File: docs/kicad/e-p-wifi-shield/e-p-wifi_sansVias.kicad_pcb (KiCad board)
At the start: 2 copper layers, 76.2 x 86.4 mm, 49 parts, among them J1 Shunt, J2 Vbat1, J3 Masse T1, J4 Température, J5 Vbat2, J6 Conn_02x14_MKR1010, SW1 StSp - Farnell 986-501, SW2 Sleep - Farnell 986-501, SW3 Conrad 711771, SW4 BP APEM - Farnell 108-2512

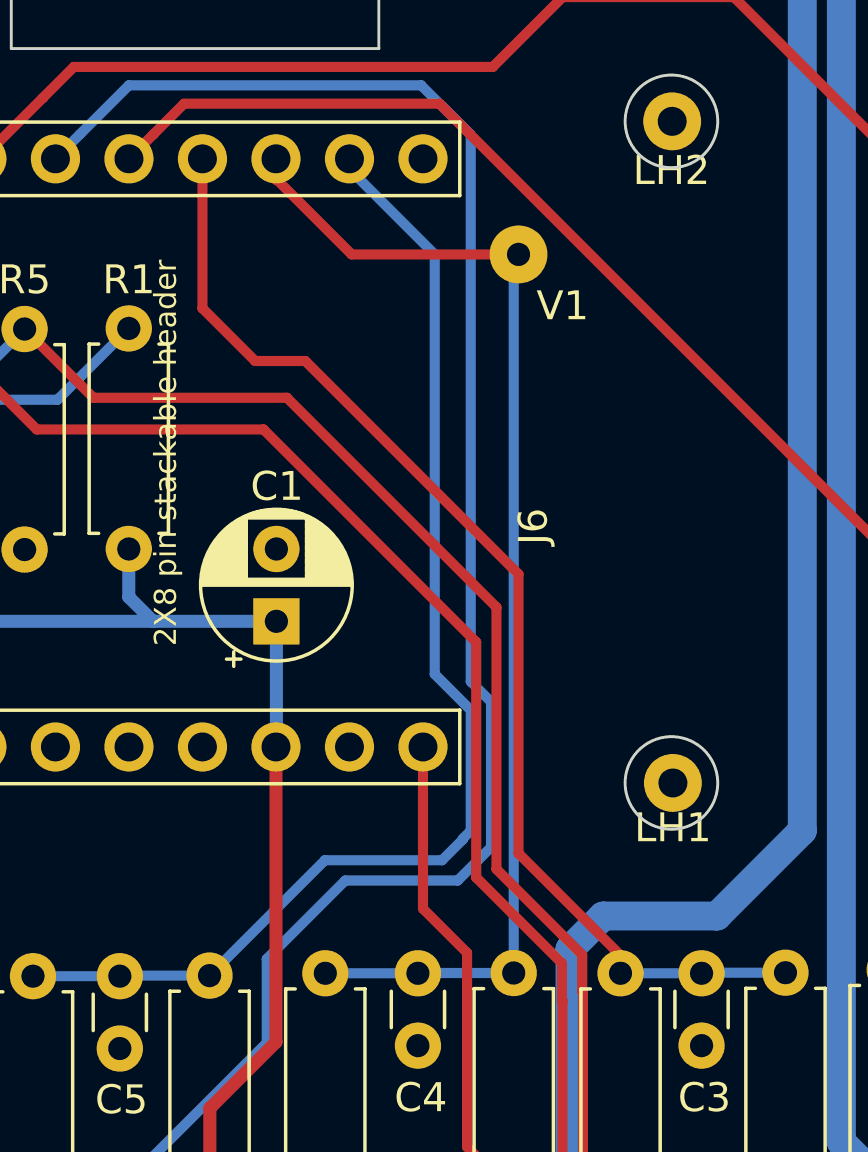
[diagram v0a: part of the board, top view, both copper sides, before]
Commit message: update schema and pcb without via
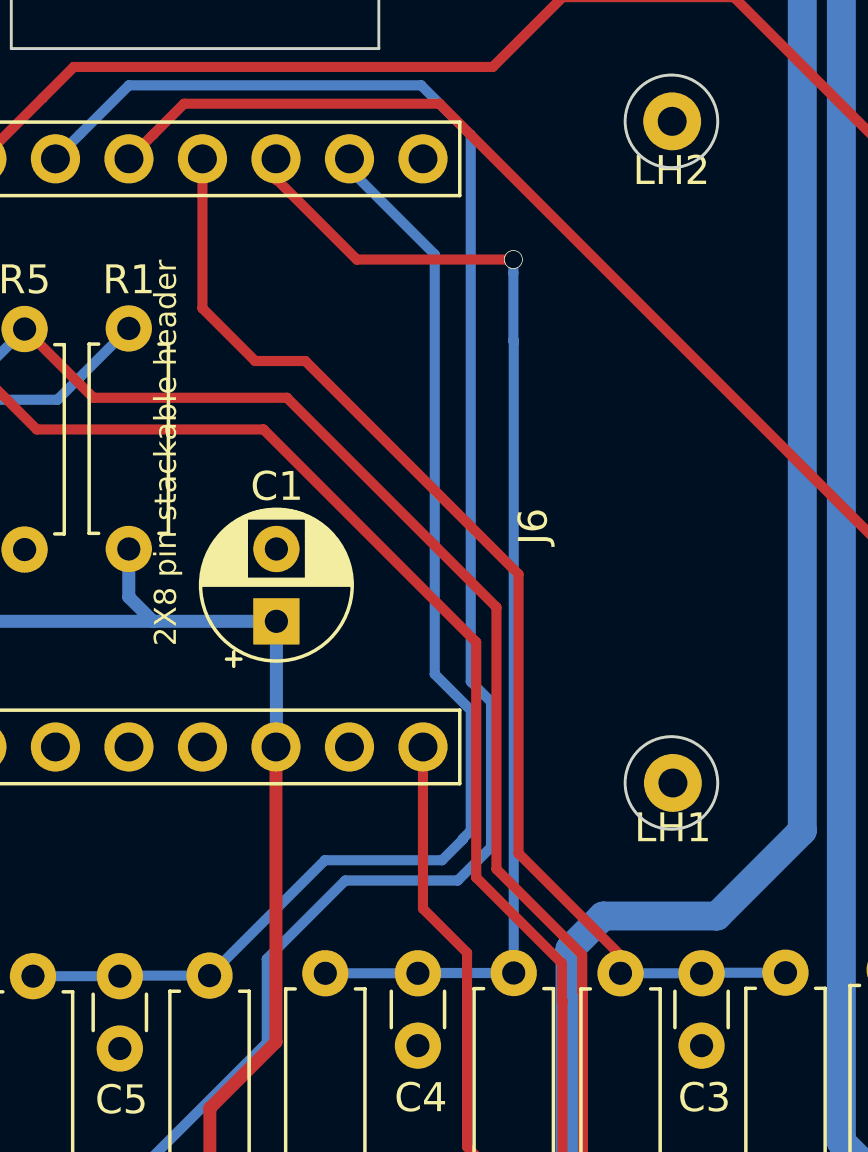
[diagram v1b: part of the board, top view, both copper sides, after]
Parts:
- removed V1: Via, e-p-wifi-v2:Via-DIY
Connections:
- SW4 pad 3: (no net) -> GND
- SW4 pad 4: (no net) -> GND
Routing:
- net Net-(C4-Pad1): track 42.3 -> 42.0 mm, vias 0 -> 1
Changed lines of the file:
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@@
     (thickness 1.6)
     (drawings 43)
-    (tracks 245)
+    (tracks 249)
     (zones 0)
-    (modules 49)
+    (modules 48)
     (nets 38)
   )
@@
     (fp_line (start 3.81 0) (end 3.81 7.62) (layer F.SilkS) (width 0.12))
     (fp_line (start -3.81 0) (end 3.81 0) (layer F.SilkS) (width 0.12))
-    (pad 3 thru_hole circle (at -2.54 5.08) (size 1.524 1.524) (drill 0.8) (layers *.Cu *.Mask))
-    (pad 4 thru_hole circle (at 2.54 5.08) (size 1.524 1.524) (drill 0.8) (layers *.Cu *.Mask))
+    (pad 3 thru_hole circle (at -2.54 5.08) (size 1.524 1.524) (drill 0.8) (layers *.Cu *.Mask)
+      (net 2 GND))
+    (pad 4 thru_hole circle (at 2.54 5.08) (size 1.524 1.524) (drill 0.8) (layers *.Cu *.Mask)
+      (net 2 GND))
     (pad 2 thru_hole circle (at 2.54 0) (size 1.524 1.524) (drill 0.8) (layers *.Cu *.Mask)
       (net 37 "Net-(C6-Pad1)"))
     (pad 1 thru_hole circle (at -2.54 0) (size 1.524 1.524) (drill 0.8) (layers *.Cu *.Mask)
       (net 1 +3V3))
-  )
-  (module e-p-wifi-v2:Via-DIY (layer F.Cu)
-    (at 70.866 61.722)
-    (descr "CP, Axial series, Axial, Horizontal, pin pitch=15mm, , length*diameter=10*4.5mm^2, Electrolytic Capacitor, , http://www.vishay.com/docs/28325/021asm.pdf")
-    (tags "CP Axial series Axial Horizontal pin pitch 15mm  length 10mm diameter 4.5mm Electrolytic Capacitor")
-    (fp_text reference V1 (at 1.524 1.778) (layer F.SilkS)
-      (effects (font (size 1 1) (thickness 0.15)))
-    )
-    (fp_text value Via (at 3.81 1.27) (layer F.Fab)
-      (effects (font (size 1 1) (thickness 0.15)))
-    )
-    (fp_text user %R (at 3.81 0) (layer F.Fab)
-      (effects (font (size 1 1) (thickness 0.15)))
-    )
-    (pad 1 thru_hole oval (at 0 0) (size 2 2) (drill 0.8) (layers *.Cu *.Mask)
-      (net 5 "Net-(C4-Pad1)"))
-    (model ${KISYS3DMOD}/Capacitor_THT.3dshapes/CP_Axial_L10.0mm_D4.5mm_P15.00mm_Horizontal.wrl
-      (at (xyz 0 0 0))
-      (scale (xyz 1 1 1))
-      (rotate (xyz 0 0 0))
-    )
   )
   (module e-p-wifi-v2:Via-DIY (layer F.Cu)
@@
   (segment (start 67.39 86.56) (end 64.19 86.56) (width 0.35) (layer B.Cu) (net 5))
   (segment (start 62.485 59.148541) (end 62.485 58.42) (width 0.35) (layer F.Cu) (net 5))
-  (segment (start 70.7 61.888) (end 70.866 61.722) (width 0.35) (layer B.Cu) (net 5))
-  (segment (start 70.7 86.55) (end 70.7 61.888) (width 0.35) (layer B.Cu) (net 5))
+  (segment (start 70.7 86.55) (end 70.7 64.7056) (width 0.35) (layer B.Cu) (net 5))
+  (segment (start 70.7 64.77) (end 70.7 64.7056) (width 0.35) (layer B.Cu) (net 5))
+  (via (at 70.6882 61.8998) (size 0.65) (drill 0.6) (layers F.Cu B.Cu) (net 5))
+  (segment (start 70.6882 62.359419) (end 70.6882 61.8998) (width 0.35) (layer B.Cu) (net 5))
+  (segment (start 70.7 64.7056) (end 70.6882 64.6938) (width 0.35) (layer B.Cu) (net 5))
+  (segment (start 70.6882 64.6938) (end 70.6882 62.359419) (width 0.35) (layer B.Cu) (net 5))
   (segment (start 62.485 59.1068) (end 62.485 58.42) (width 0.35) (layer F.Cu) (net 5))
-  (segment (start 70.866 61.722) (end 65.1002 61.722) (width 0.35) (layer F.Cu) (net 5))
-  (segment (start 65.1002 61.722) (end 62.485 59.1068) (width 0.35) (layer F.Cu) (net 5))
+  (segment (start 70.6882 61.8998) (end 65.278 61.8998) (width 0.35) (layer F.Cu) (net 5))
+  (segment (start 65.278 61.8998) (end 62.485 59.1068) (width 0.35) (layer F.Cu) (net 5))
   (segment (start 57.11 86.64) (end 57.09 86.66) (width 0.35) (layer B.Cu) (net 6))
   (segment (start 60.19 86.64) (end 57.11 86.64) (width 0.35) (layer B.Cu) (net 6))
